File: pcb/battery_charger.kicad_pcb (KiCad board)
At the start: 2 copper layers, 50 x 50 mm, 20 parts, among them J1 USB_B_Micro, J2 IN+, J3 IN-, J4 OUT+, J5 BAT+, J6 BAT-, J7 OUT-, U1 TP4056, U2 DW01A, U3 FS8205A

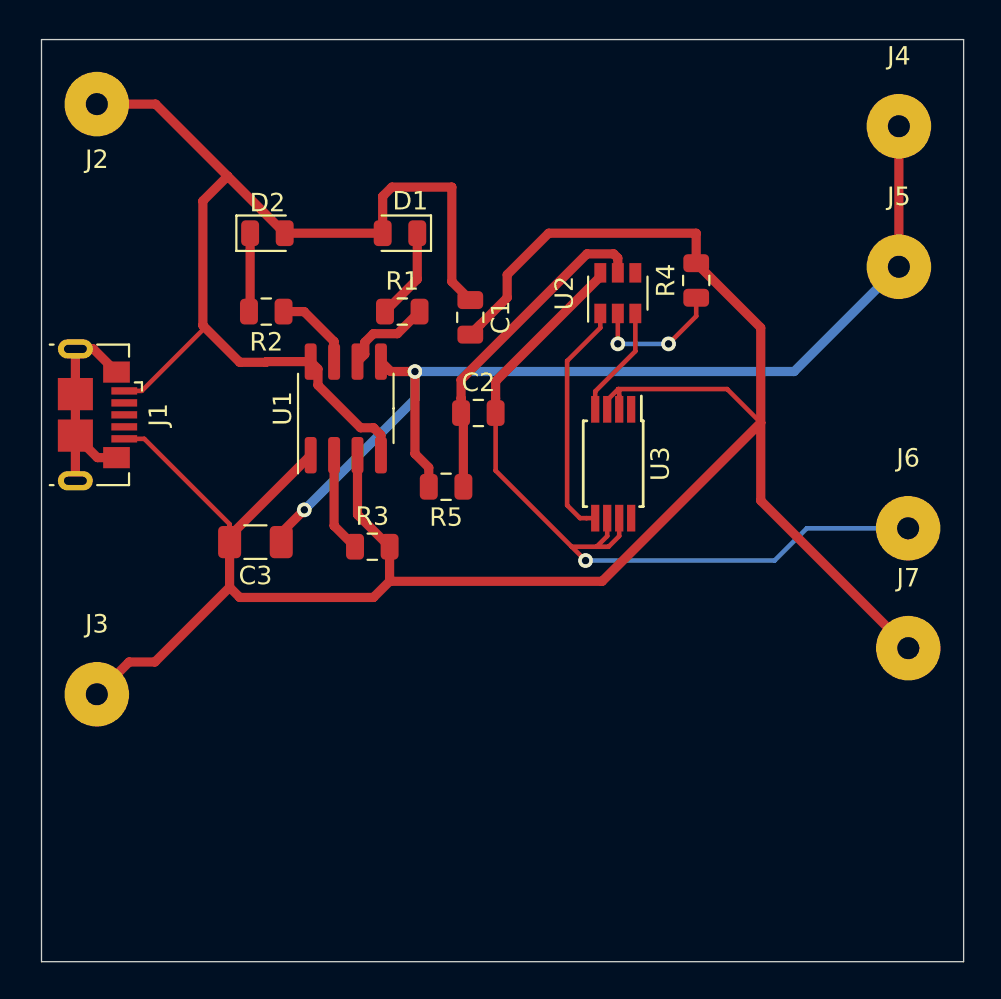
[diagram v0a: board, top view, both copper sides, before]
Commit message: Se optimiza el area ocupada por el pcb
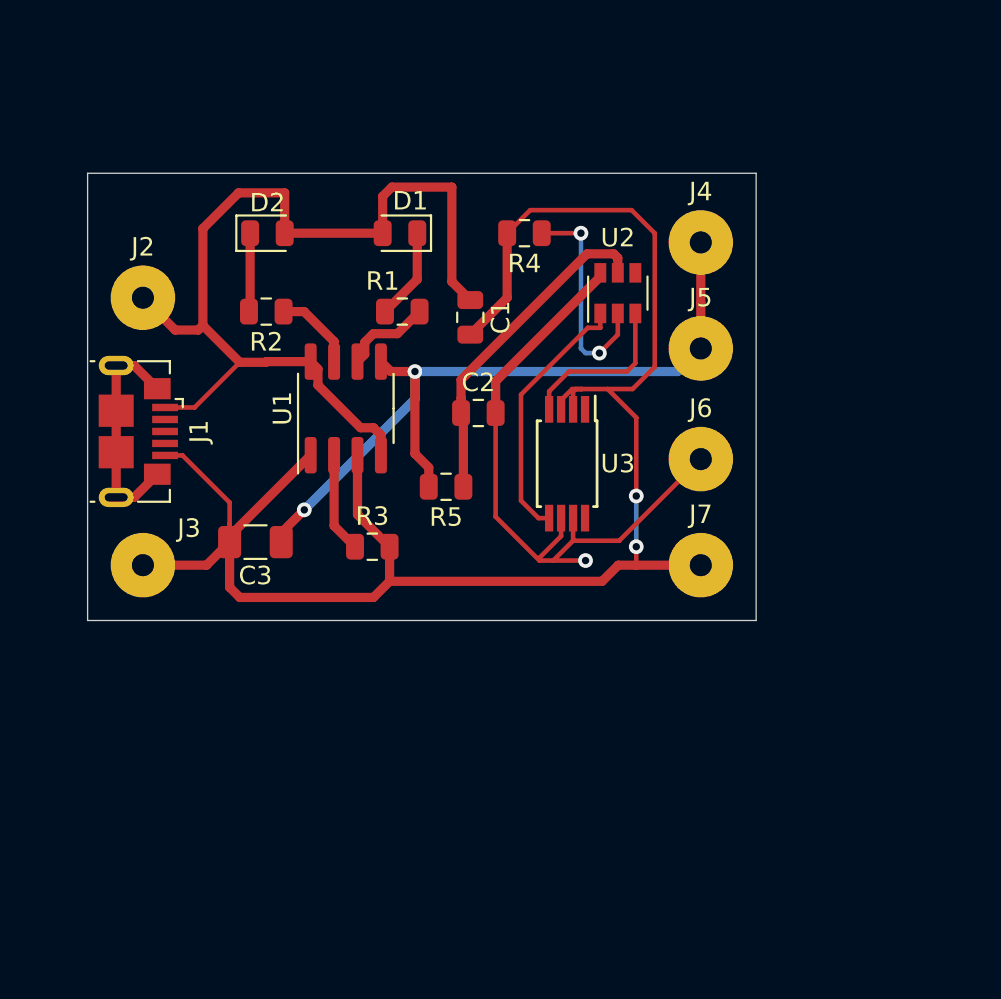
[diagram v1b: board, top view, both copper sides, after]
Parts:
- moved J4 12.5 mm to (135.8, 121.0)
- moved J7 12.1 mm to (135.8, 138.5)
- moved J6 11.8 mm to (135.8, 132.8)
- moved J5 11.6 mm to (135.8, 126.8)
- moved J2 10.8 mm to (105.5, 124.0)
- moved R4 9.66 mm to (126.2, 120.5), turned to 180 degrees
- moved J3 7.43 mm to (105.5, 138.5)
- moved U3 2.50 mm to (128.5, 133.0)
- moved J1 2.39 mm to (105.2, 131.2)
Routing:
- net GND: track 122.7 -> 95.6 mm, vias 0 -> 2
- net Net-(C3-Pad1): track 57.1 -> 42.6 mm
- net Net-(C2-Pad2): track 43.8 -> 35.7 mm
- net +5V: track 59.2 -> 53.4 mm
- net Net-(R4-Pad1): track 7.52 -> 12.0 mm
- net Net-(U2-Pad3): track 6.10 -> 8.98 mm
- net Net-(U2-Pad1): track 13.0 -> 14.2 mm
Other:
- board size 50 x 50 mm -> 36.2 x 24.2 mm

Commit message: Se agrega relleno de cobre
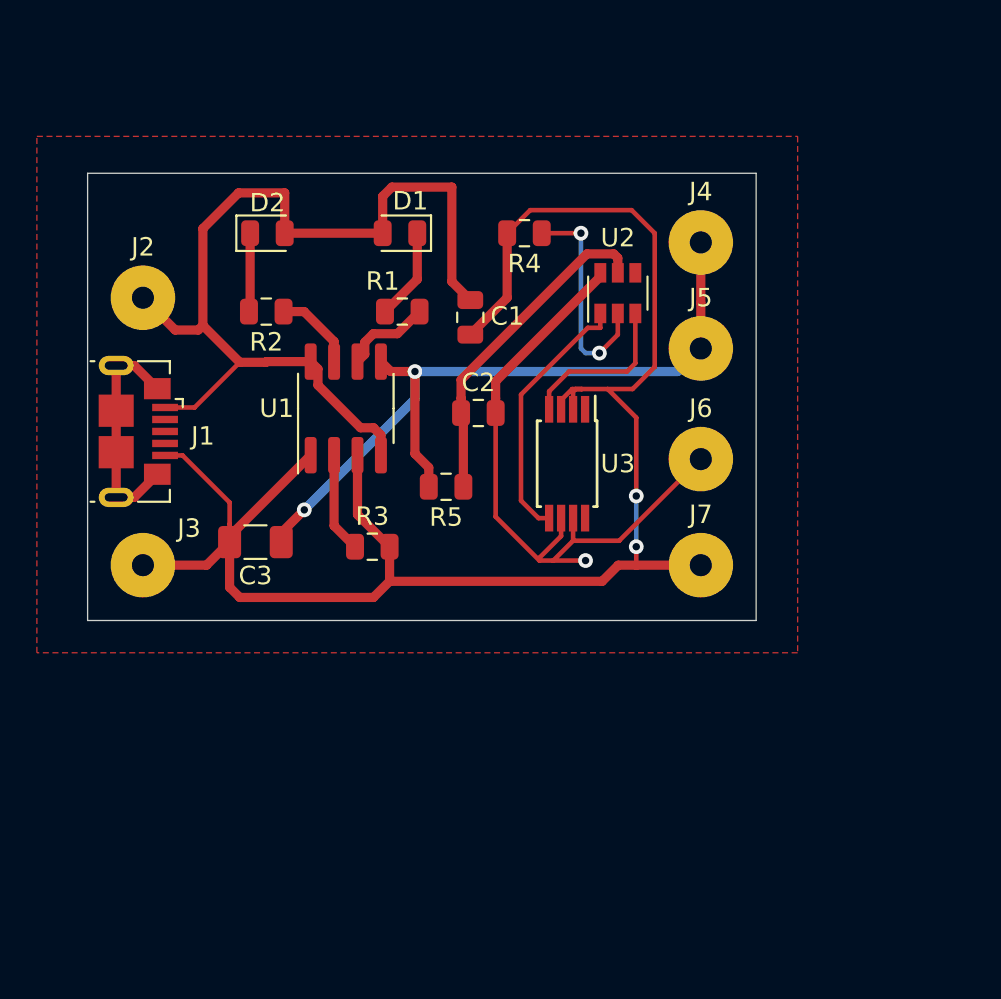
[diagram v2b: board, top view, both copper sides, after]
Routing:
- added copper zone on F.Cu, net GND
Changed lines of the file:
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@@
     (clearance 0.1)
     (attr smd)
-    (fp_text reference J1 (at 0 -3.3 90) (layer F.SilkS)
+    (fp_text reference J1 (at 0.25 -3.5 180) (layer F.SilkS)
       (effects (font (size 1 1) (thickness 0.15)))
     )
@@
     (tags "SOP SO")
     (attr smd)
-    (fp_text reference U1 (at 0 -3.43 90) (layer F.SilkS)
+    (fp_text reference U1 (at 0 -3.75 180) (layer F.SilkS)
       (effects (font (size 1 1) (thickness 0.15)))
     )
@@
     (tags capacitor)
     (attr smd)
-    (fp_text reference C1 (at 0 -1.65 90) (layer F.SilkS)
+    (fp_text reference C1 (at -0.0625 -2 180) (layer F.SilkS)
       (effects (font (size 1 1) (thickness 0.15)))
     )
@@
   (segment (start 128.599998 128) (end 127.525 129.075) (width 0.25) (layer F.Cu) (net 17))
   (segment (start 131.75 128) (end 128.599998 128) (width 0.25) (layer F.Cu) (net 17))
+  (zone (net 2) (net_name GND) (layer F.Cu) (hatch edge 0.508)
+    (connect_pads (clearance 0.508))
+    (min_thickness 0.254)
+    (fill yes (arc_segments 32) (thermal_gap 0.508) (thermal_bridge_width 0.508))
+    (polygon
+      (pts
+        (xy 99.75 115.25) (xy 141 115.25) (xy 141 143.25) (xy 99.75 143.25)
+      )
+    )
+  )
 )

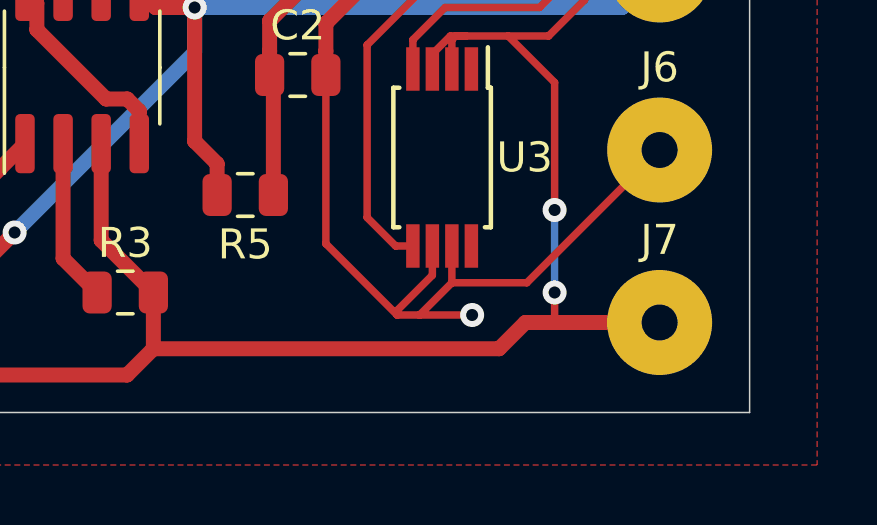
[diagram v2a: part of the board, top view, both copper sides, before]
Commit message: Se elimina via innecesaria
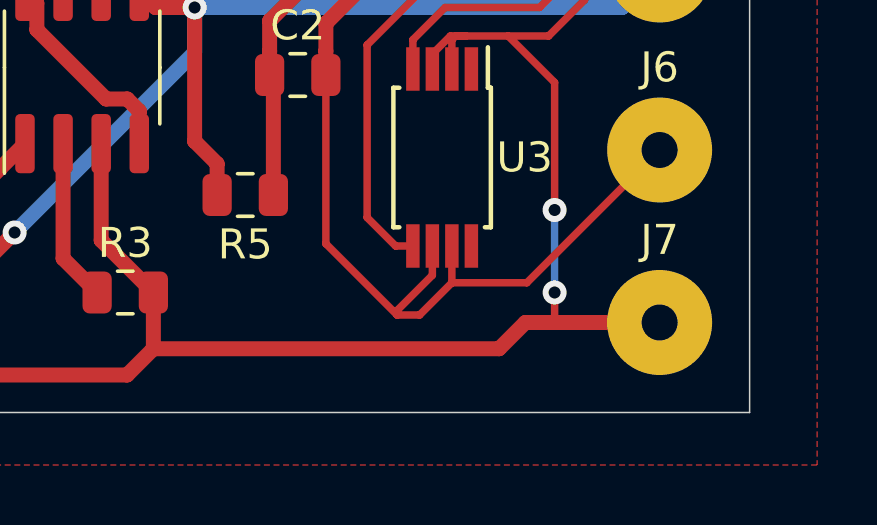
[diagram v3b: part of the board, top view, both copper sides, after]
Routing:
- net Net-(C2-Pad2): track 35.7 -> 34.0 mm, vias 1 -> 0
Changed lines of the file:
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@@
     (thickness 1.6)
     (drawings 4)
-    (tracks 144)
+    (tracks 142)
     (zones 0)
     (modules 20)
@@
   (segment (start 130.3 122.855) (end 124.625 128.53) (width 0.5) (layer F.Cu) (net 3))
   (segment (start 130.3 122.65) (end 130.3 122.855) (width 0.5) (layer F.Cu) (net 3))
-  (via (at 129.5 138.25) (size 0.8) (drill 0.4) (layers F.Cu B.Cu) (net 3))
   (segment (start 124.625 130.25) (end 124.625 135.875) (width 0.25) (layer F.Cu) (net 3))
   (segment (start 124.625 135.875) (end 127 138.25) (width 0.25) (layer F.Cu) (net 3))
@@
   (segment (start 128.825 135.95) (end 128.825 137.175) (width 0.25) (layer F.Cu) (net 3))
   (segment (start 127 138.25) (end 127.75 138.25) (width 0.25) (layer F.Cu) (net 3))
-  (segment (start 127.75 138.25) (end 129.5 138.25) (width 0.25) (layer F.Cu) (net 3))
   (segment (start 131.325 137.175) (end 135.75 132.75) (width 0.25) (layer F.Cu) (net 3))
   (segment (start 128.825 137.175) (end 131.325 137.175) (width 0.25) (layer F.Cu) (net 3))
